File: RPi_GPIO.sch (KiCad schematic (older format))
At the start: 39 parts, among them J2 RPi_GPIO, J3 Conn_02x03_Counter_Clockwise, J4 Conn_01x02_Male, J5 Conn_01x03_Male, J6 Conn_01x03_Male, J7 Conn_01x03_Male, J8 Conn_01x03_Male, SW1 SW_Push, U2 STM32F030CCTx, U3 MAX485E, U4 MAX485E, U5 MAX485E, U6 MAX485E

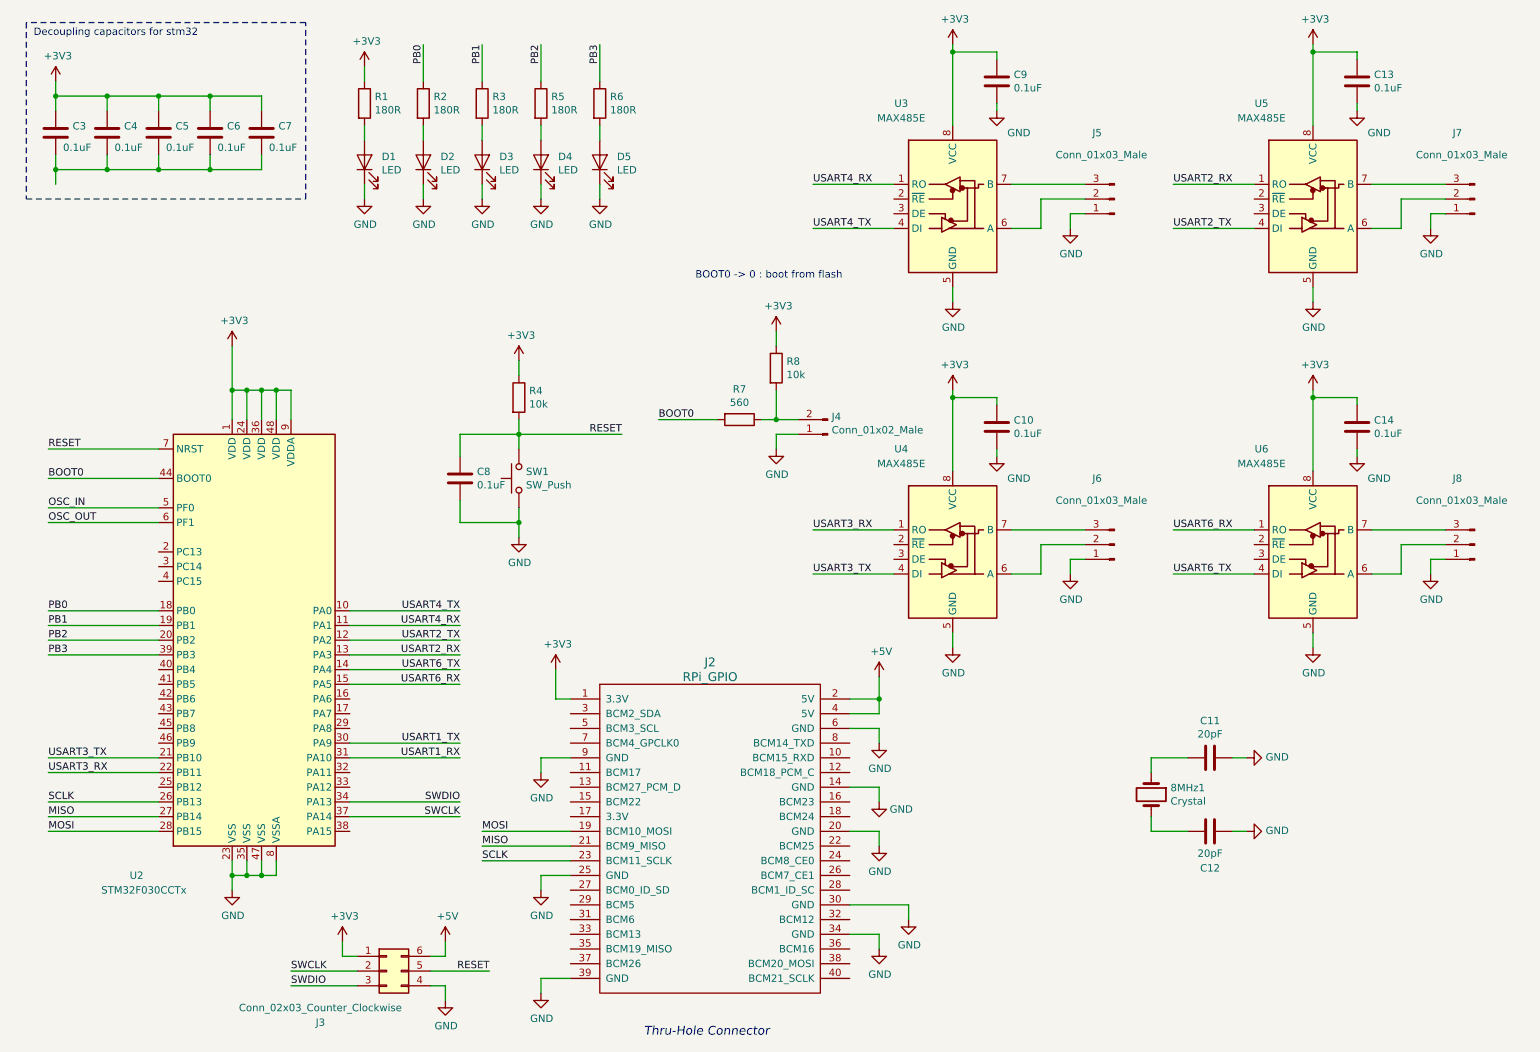
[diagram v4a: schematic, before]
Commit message: Correct DRC and add nmea interface
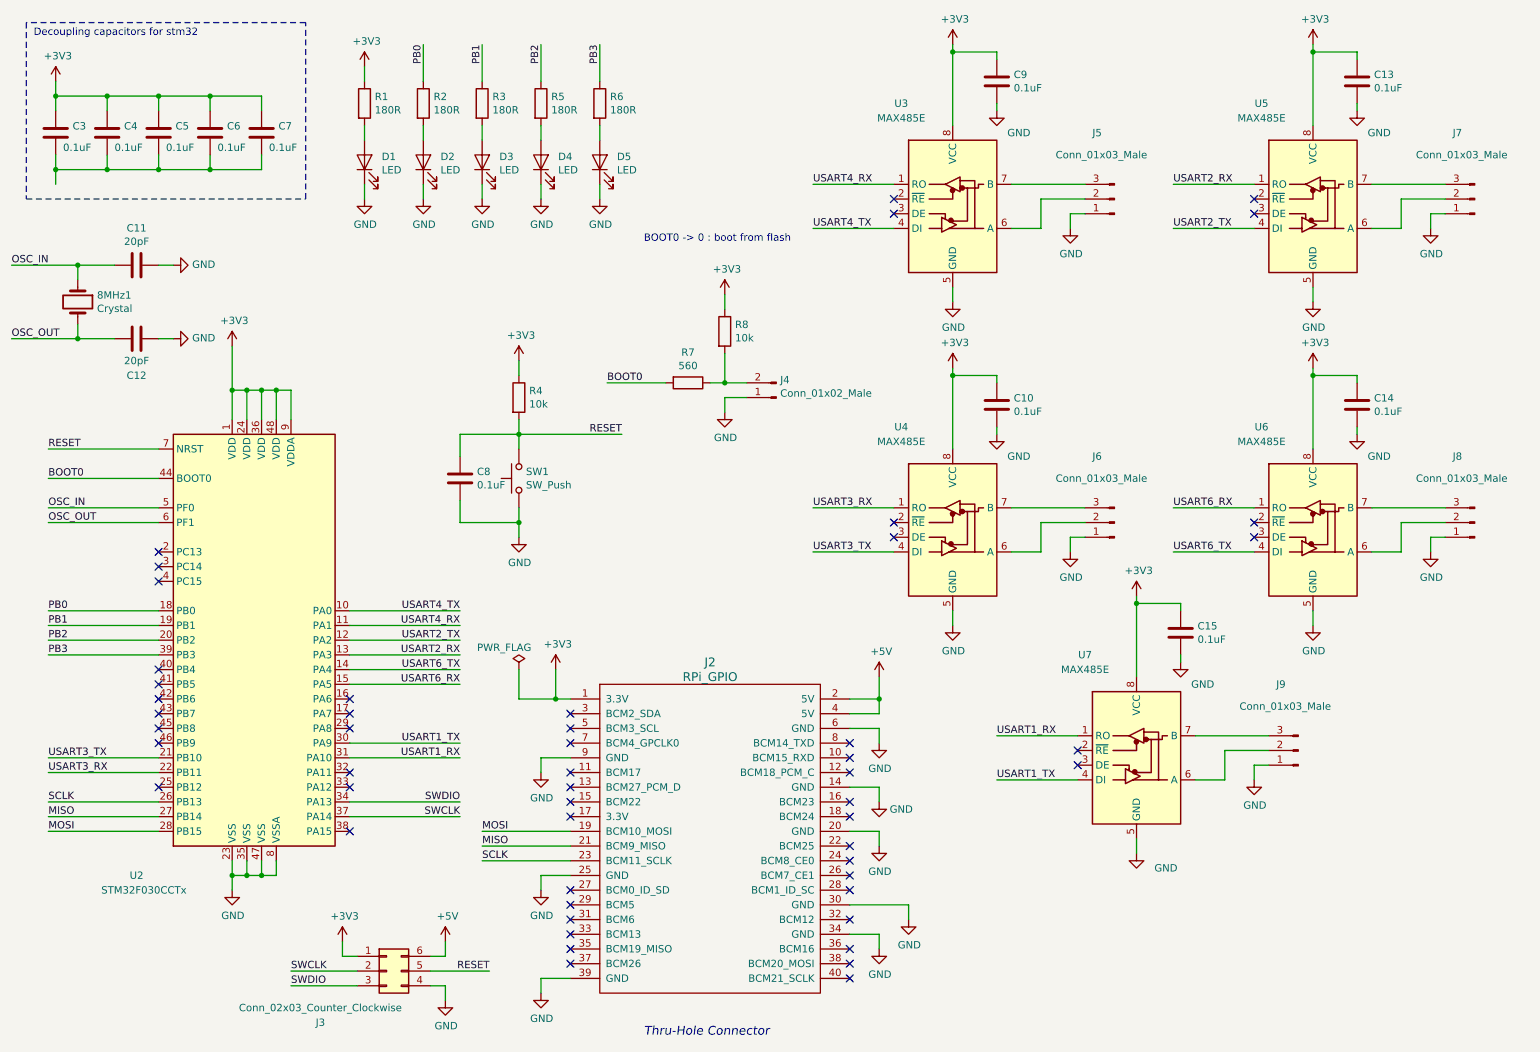
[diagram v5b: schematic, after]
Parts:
- added C15: 0.1uF, Capacitors_SMD:C_0603_HandSoldering, symbol Device:C
- added J9: Conn_01x03_Male, Connectors_JST:JST_ACH_BM03B-ACHSS_03x1.20mm_Angled, symbol Connector:Conn_01x03_Male
- added U7: MAX485E, digikey-footprints:SOIC-8_W3.9mm, symbol Interface_UART:MAX485E
- J5, J6, J7, J8: footprint (none) -> Connectors_JST:JST_ACH_BM03B-ACHSS_03x1.20mm_Angled; dkReference ED2819-ND -> 455-1579-1-ND
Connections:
- net +3V3: now also C15.1, U7.8 (VCC)
- net GND: now also C15.2, J9.1 (Pin_1), U7.5 (GND)
- net OSC_IN: now also 8MHz1.1, C11.2
- net OSC_OUT: now also 8MHz1.2, C12.2
- net USART1_RX: now also U7.1 (RO)
- net USART1_TX: now also U7.4 (DI)
- new net: J9.2 (Pin_2), U7.6 (A)
- new net: J9.3 (Pin_3), U7.7 (B)
- no-connect marks 0 -> 52
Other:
- moved on the sheet: 8MHz1, C10, C11, C12, C14, J4, J6, J8, R7, R8, U4, U6

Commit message: Finish schem and start routing
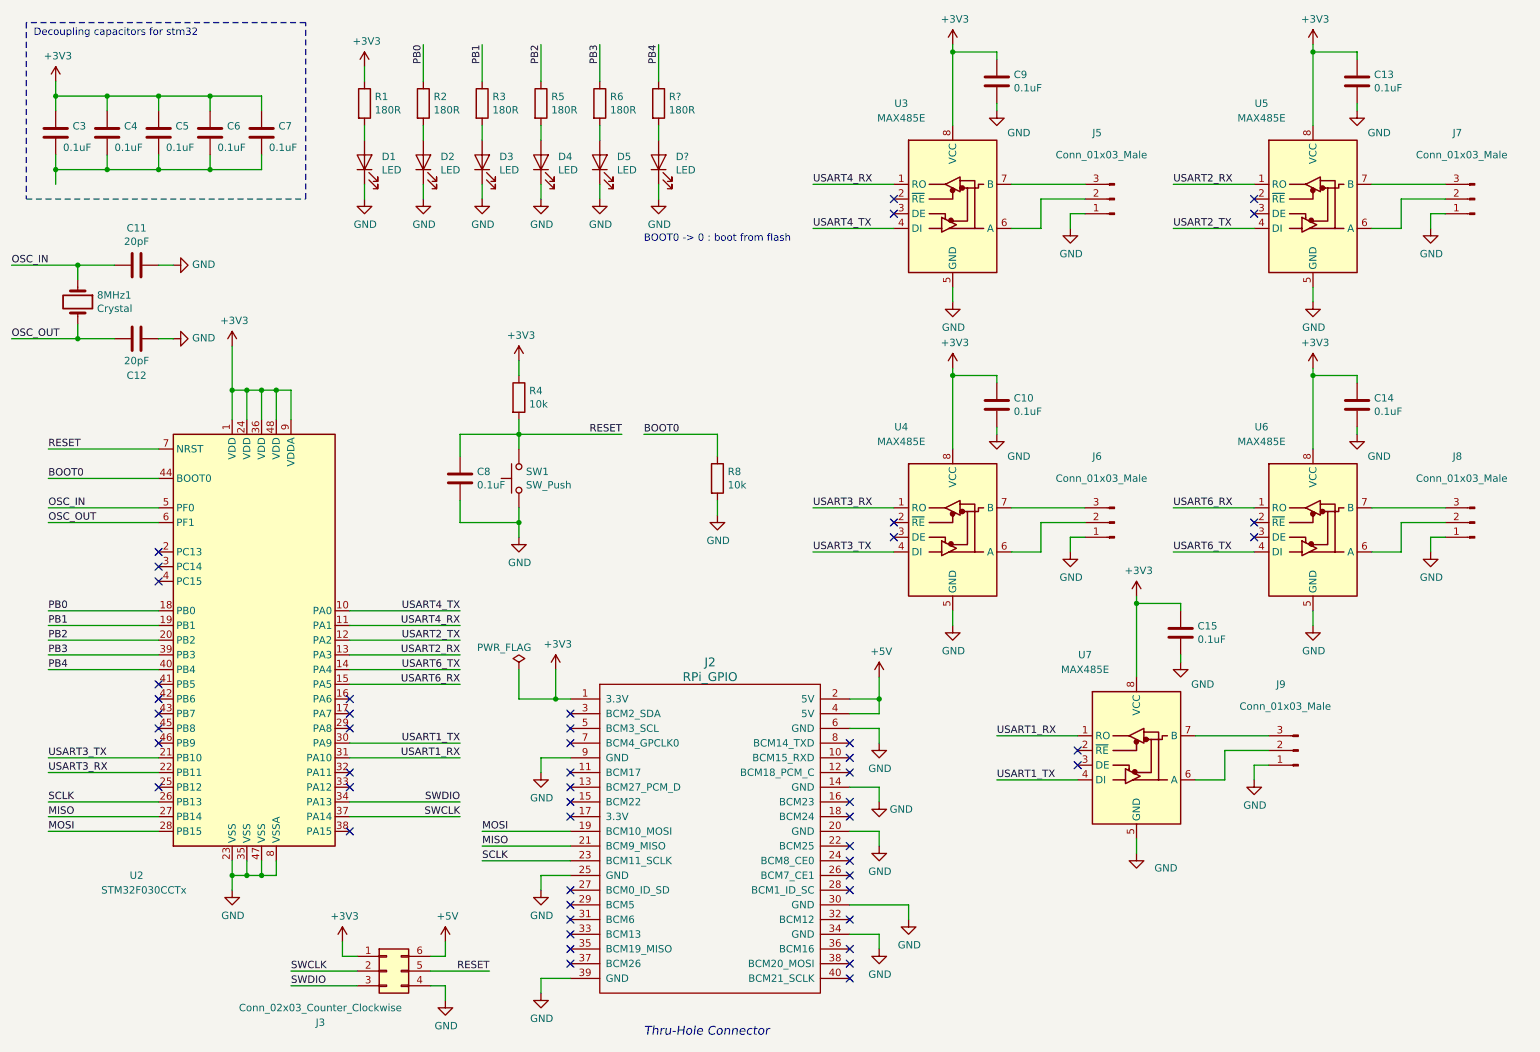
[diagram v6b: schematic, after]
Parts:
- removed J4: Conn_01x02_Male, symbol Connector:Conn_01x02_Male
- removed R7: 560, LEDs:LED_0603_HandSoldering, symbol Device:R
- added D?: LED, LEDs:LED_0603_HandSoldering, symbol Device:LED
- added R?: 180R, Resistors_SMD:R_0603_HandSoldering, symbol Device:R
- J3: footprint (none) -> Connectors_Samtec:SDL-106-X-XX_2x03
- J5, J6, J7, J8, J9: footprint Connectors_JST:JST_ACH_BM03B-ACHSS_03x1.20mm_Angled -> Connectors_JST:JST_SH_SM03B-SRSS-TB_03x1.00mm_Angled; dkReference 455-1579-1-ND -> 455-1803-1-ND
- U2: footprint Package_QFP:LQFP-48_7x7mm_P0.5mm -> digikey-footprints:LQFP-48_7x7mm
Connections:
- net +3V3: no longer R8.1
- net BOOT0: now also R8.1
- net GND: now also R8.2, D?.1 (K)
- net PB4: now reaches U2.40 (PB4)
- net PB4: now also R?.1
- new net: D?.2 (A), R?.2
- no-connect marks 52 -> 51
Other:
- moved on the sheet: R8
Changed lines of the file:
@@
 F 0 "U2" H 1550 3300 50  0000 C CNN
 F 1 "STM32F030CCTx" H 1600 3200 50  0000 C CNN
-F 2 "Package_QFP:LQFP-48_7x7mm_P0.5mm" H 1800 3500 50  0001 R CNN
+F 2 "digikey-footprints:LQFP-48_7x7mm" H 1800 3500 50  0001 R CNN
 F 3 "http://www.st.com/st-web-ui/static/active/en/resource/technical/document/datasheet/DM00088500.pdf" H 2400 4900 50  0001 C CNN
 F 4 "497-17296-ND" H 2400 4900 50  0001 C CNN "dkReference"
@@
 Text Label 950  3800 0    50   ~ 0
 BOOT0
-$Comp
-L power:GND #PWR?
-U 1 1 5C4AB0B1
-P 5550 3350
-F 0 "#PWR?" H 5550 3100 50  0001 C CNN
-F 1 "GND" H 5555 3177 50  0000 C CNN
-F 2 "" H 5550 3350 50  0001 C CNN
-F 3 "" H 5550 3350 50  0001 C CNN
-	1    5550 3350
-	1    0    0    -1
-$EndComp
 Text Notes 6000 2200 2    50   ~ 0
 BOOT0 -> 0 : boot from flash
@@
 F 0 "J5" H 8350 1450 50  0000 R CNN
 F 1 "Conn_01x03_Male" H 8600 1600 50  0000 R CNN
-F 2 "Connectors_JST:JST_ACH_BM03B-ACHSS_03x1.20mm_Angled" H 8200 1900 50  0001 C CNN
+F 2 "Connectors_JST:JST_SH_SM03B-SRSS-TB_03x1.00mm_Angled" H 8200 1900 50  0001 C CNN
 F 3 "~" H 8200 1900 50  0001 C CNN
-F 4 "455-1579-1-ND" H 0   0   50  0001 C CNN "dkReference"
+F 4 "455-1803-1-ND" H 0   0   50  0001 C CNN "dkReference"
 	1    8200 1900
 	-1   0    0    1
@@
 F 0 "J7" H 10800 1450 50  0000 R CNN
 F 1 "Conn_01x03_Male" H 11050 1600 50  0000 R CNN
-F 2 "Connectors_JST:JST_ACH_BM03B-ACHSS_03x1.20mm_Angled" H 10650 1900 50  0001 C CNN
+F 2 "Connectors_JST:JST_SH_SM03B-SRSS-TB_03x1.00mm_Angled" H 10650 1900 50  0001 C CNN
 F 3 "~" H 10650 1900 50  0001 C CNN
-F 4 "455-1579-1-ND" H 0   0   50  0001 C CNN "dkReference"
+F 4 "455-1803-1-ND" H 0   0   50  0001 C CNN "dkReference"
 	1    10650 1900
 	-1   0    0    1
@@
 F 0 "J6" H 8350 3650 50  0000 R CNN
 F 1 "Conn_01x03_Male" H 8600 3800 50  0000 R CNN
-F 2 "Connectors_JST:JST_ACH_BM03B-ACHSS_03x1.20mm_Angled" H 8200 4100 50  0001 C CNN
+F 2 "Connectors_JST:JST_SH_SM03B-SRSS-TB_03x1.00mm_Angled" H 8200 4100 50  0001 C CNN
 F 3 "~" H 8200 4100 50  0001 C CNN
-F 4 "455-1579-1-ND" H 0   -150 50  0001 C CNN "dkReference"
+F 4 "455-1803-1-ND" H 0   -150 50  0001 C CNN "dkReference"
 	1    8200 4100
 	-1   0    0    1
@@
 F 0 "J8" H 10800 3650 50  0000 R CNN
 F 1 "Conn_01x03_Male" H 11050 3800 50  0000 R CNN
-F 2 "Connectors_JST:JST_ACH_BM03B-ACHSS_03x1.20mm_Angled" H 10650 4100 50  0001 C CNN
+F 2 "Connectors_JST:JST_SH_SM03B-SRSS-TB_03x1.00mm_Angled" H 10650 4100 50  0001 C CNN
 F 3 "~" H 10650 4100 50  0001 C CNN
-F 4 "455-1579-1-ND" H 0   -150 50  0001 C CNN "dkReference"
+F 4 "455-1803-1-ND" H 0   -150 50  0001 C CNN "dkReference"
 	1    10650 4100
 	-1   0    0    1
@@
 F 0 "J3" H 2800 6800 50  0000 C CNN
 F 1 "Conn_02x03_Counter_Clockwise" H 2800 6900 50  0000 C CNN
-F 2 "" H 3250 7150 50  0001 C CNN
+F 2 "Connectors_Samtec:SDL-106-X-XX_2x03" H 3250 7150 50  0001 C CNN
 F 3 "~" H 3250 7150 50  0001 C CNN
 	1    3250 7150
@@
 	1    0    0    -1
 $EndComp
-Text Label 4750 3150 0    50   ~ 0
+Text Label 5000 3500 0    50   ~ 0
 BOOT0
-Wire Wire Line
-	5550 3250 5550 3350
 $Comp
 L Device:R R8
 U 1 1 5C658078
-P 5550 2800
-F 0 "R8" H 5620 2846 50  0000 L CNN
-F 1 "10k" H 5620 2755 50  0000 L CNN
-F 2 "Resistors_SMD:R_0603_HandSoldering" V 5480 2800 50  0001 C CNN
-F 3 "~" H 5550 2800 50  0001 C CNN
-F 4 "RMCF0201FT10K0CT-ND" H 5550 2800 50  0001 C CNN "dkReference"
-	1    5550 2800
-	1    0    0    -1
-$EndComp
-Wire Wire Line
-	5550 2650 5550 2550
-$Comp
-L power:+3V3 #PWR?
-U 1 1 5C66017C
-P 5550 2550
-F 0 "#PWR?" H 5550 2400 50  0001 C CNN
-F 1 "+3V3" H 5565 2723 50  0000 C CNN
-F 2 "" H 5550 2550 50  0001 C CNN
-F 3 "" H 5550 2550 50  0001 C CNN
-	1    5550 2550
+P 5500 3800
+F 0 "R8" H 5570 3846 50  0000 L CNN
+F 1 "10k" H 5570 3755 50  0000 L CNN
+F 2 "Resistors_SMD:R_0603_HandSoldering" V 5430 3800 50  0001 C CNN
+F 3 "~" H 5500 3800 50  0001 C CNN
+F 4 "RMCF0201FT10K0CT-ND" H 5500 3800 50  0001 C CNN "dkReference"
+	1    5500 3800
 	1    0    0    -1
 $EndComp
@@
 	0    -1   -1   0
 $EndComp
-Wire Wire Line
-	5550 2950 5550 3150
-$Comp
-L Connector:Conn_01x02_Male J4
-U 1 1 5C6B4A6B
-P 5900 3250
-F 0 "J4" H 5873 3130 50  0000 R CNN
-F 1 "Conn_01x02_Male" H 5873 3221 50  0000 R CNN
-F 2 "" H 5900 3250 50  0001 C CNN
-F 3 "~" H 5900 3250 50  0001 C CNN
-F 4 "ED2819-ND" H -350 -250 50  0001 C CNN "dkReference"
-	1    5900 3250
-	-1   0    0    1
-$EndComp
-Wire Wire Line
-	5700 3150 5550 3150
-Wire Wire Line
-	5550 3250 5700 3250
-Wire Wire Line
-	5550 3150 5450 3150
-Connection ~ 5550 3150
-$Comp
-L Device:R R7
-U 1 1 5C6D6442
-P 5300 3150
-F 0 "R7" V 5093 3150 50  0000 C CNN
-F 1 "560" V 5184 3150 50  0000 C CNN
-F 2 "LEDs:LED_0603_HandSoldering" V 5230 3150 50  0001 C CNN
-F 3 "~" H 5300 3150 50  0001 C CNN
-F 4 "RC0201JR-07560RL" V 5300 3150 50  0001 C CNN "dkReference"
-	1    5300 3150
-	0    1    1    0
-$EndComp
-Wire Wire Line
-	5150 3150 4750 3150
 NoConn ~ 6400 5600
 NoConn ~ 6400 5700
@@
 NoConn ~ 1700 5300
 NoConn ~ 1700 5200
-NoConn ~ 1700 5100
 NoConn ~ 1700 4500
 NoConn ~ 1700 4400
@@
 F 0 "J9" H 9600 5200 50  0000 R CNN
 F 1 "Conn_01x03_Male" H 9850 5350 50  0000 R CNN
-F 2 "Connectors_JST:JST_ACH_BM03B-ACHSS_03x1.20mm_Angled" H 9450 5650 50  0001 C CNN
+F 2 "Connectors_JST:JST_SH_SM03B-SRSS-TB_03x1.00mm_Angled" H 9450 5650 50  0001 C CNN
 F 3 "~" H 9450 5650 50  0001 C CNN
-F 4 "455-1579-1-ND" H -1200 1400 50  0001 C CNN "dkReference"
+F 4 "455-1803-1-ND" H -1200 1400 50  0001 C CNN "dkReference"
 	1    9450 5650
 	-1   0    0    1
@@
 	1    0    0    -1
 $EndComp
+Wire Wire Line
+	5500 3500 5500 3650
+Wire Wire Line
+	5000 3500 5500 3500
+Wire Wire Line
+	5500 3950 5500 4050
+$Comp
+L power:GND #PWR?
+U 1 1 5C736817
+P 5500 4050
+F 0 "#PWR?" H 5500 3800 50  0001 C CNN
+F 1 "GND" H 5505 3877 50  0000 C CNN
+F 2 "" H 5500 4050 50  0001 C CNN
+F 3 "" H 5500 4050 50  0001 C CNN
+	1    5500 4050
+	1    0    0    -1
+$EndComp
+$Comp
+L Device:R R?
+U 1 1 5C528FF5
+P 5100 1250
+F 0 "R?" H 5170 1296 50  0000 L CNN
+F 1 "180R" H 5170 1205 50  0000 L CNN
+F 2 "Resistors_SMD:R_0603_HandSoldering" V 5030 1250 50  0001 C CNN
+F 3 "~" H 5100 1250 50  0001 C CNN
+F 4 "YAG2450CT-ND" H 5100 1250 50  0001 C CNN "dkReference"
+	1    5100 1250
+	1    0    0    -1
+$EndComp
+Wire Wire Line
+	5100 1100 5100 850
+Wire Wire Line
+	5100 1400 5100 1500
+$Comp
+L Device:LED D?
+U 1 1 5C528FFF
+P 5100 1650
+F 0 "D?" V 5138 1533 50  0000 R CNN
+F 1 "LED" V 5047 1533 50  0000 R CNN
+F 2 "LEDs:LED_0603_HandSoldering" H 5100 1650 50  0001 C CNN
+F 3 "~" H 5100 1650 50  0001 C CNN
+F 4 "SML-D12U1WT86CT-ND" V 5100 1650 50  0001 C CNN "dkReference"
+	1    5100 1650
+	0    -1   -1   0
+$EndComp
+Wire Wire Line
+	5100 1800 5100 1900
+$Comp
+L power:GND #PWR?
+U 1 1 5C529007
+P 5100 1900
+F 0 "#PWR?" H 5100 1650 50  0001 C CNN
+F 1 "GND" H 5105 1727 50  0000 C CNN
+F 2 "" H 5100 1900 50  0001 C CNN
+F 3 "" H 5100 1900 50  0001 C CNN
+	1    5100 1900
+	1    0    0    -1
+$EndComp
+Text Label 5100 850  3    50   ~ 0
+PB4
+Wire Wire Line
+	1700 5100 950  5100
+Text Label 950  5100 0    50   ~ 0
+PB4
 $EndSCHEMATC

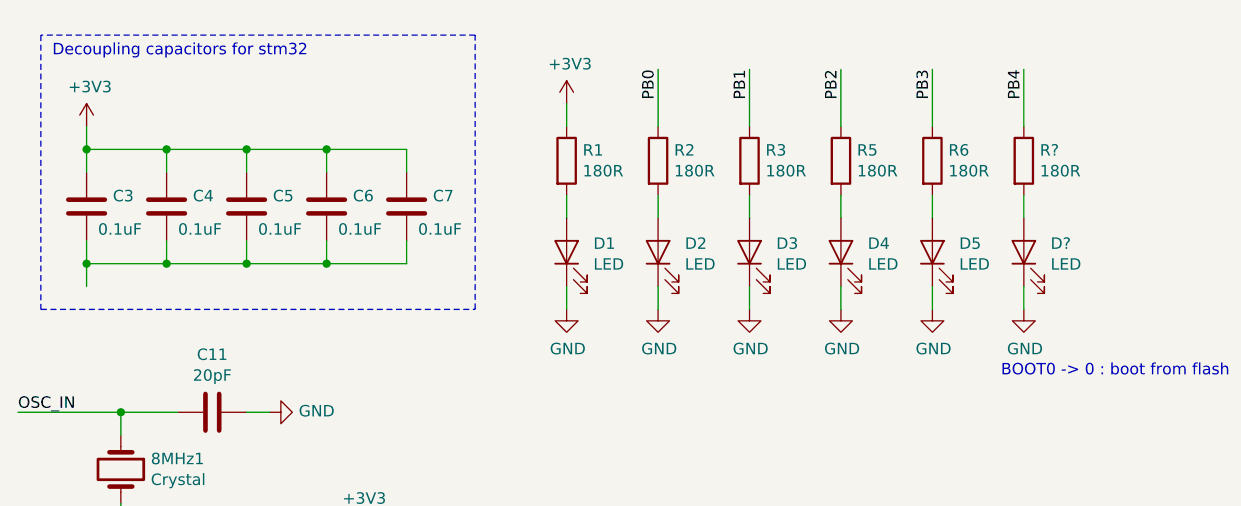
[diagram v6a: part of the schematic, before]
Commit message: Update footprints, fix gnd missing, start to align connectors
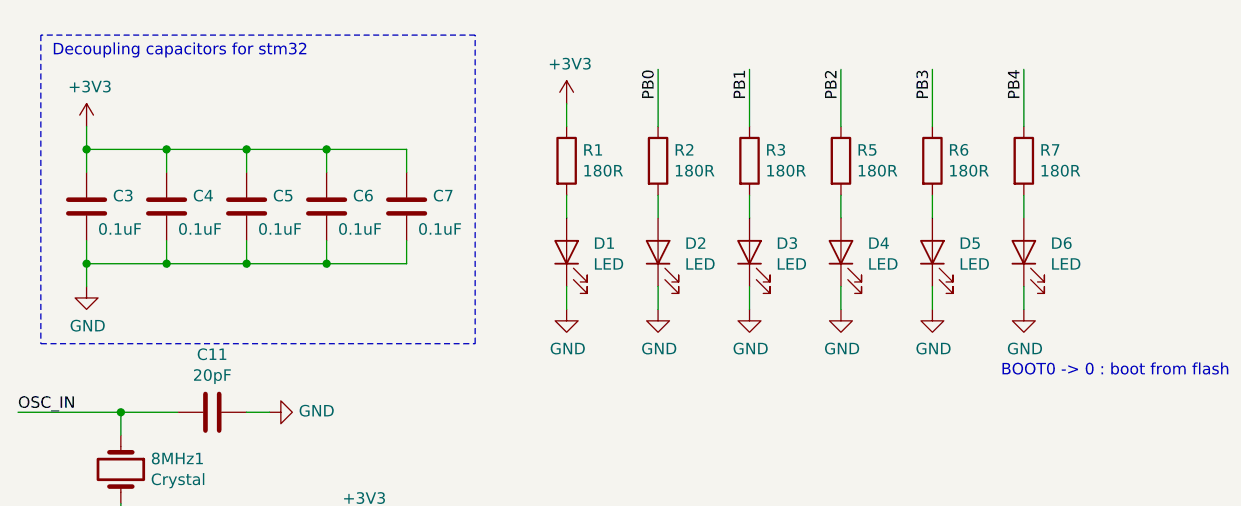
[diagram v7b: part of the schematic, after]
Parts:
- gave numbers to parts that had none: 2
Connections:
- net GND: now also C3.2, C4.2, C5.2, C6.2, C7.2
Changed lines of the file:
@@
 	1350 1700 1700 1700
 Wire Notes Line
-	800  1900 2700 1900
+	800  2050 2700 2050
 Wire Notes Line
-	2700 1900 2700 700
+	2700 2050 2700 700
 Wire Notes Line
 	2700 700  800  700
 Wire Notes Line
-	800  700  800  1900
+	800  700  800  2050
 Text Notes 850  800  0    50   ~ 0
 Decoupling capacitors for stm32\n
@@
 $EndComp
 $Comp
-L Device:R R?
+L Device:R R7
 U 1 1 5C528FF5
 P 5100 1250
-F 0 "R?" H 5170 1296 50  0000 L CNN
+F 0 "R7" H 5170 1296 50  0000 L CNN
 F 1 "180R" H 5170 1205 50  0000 L CNN
 F 2 "Resistors_SMD:R_0603_HandSoldering" V 5030 1250 50  0001 C CNN
@@
 	5100 1400 5100 1500
 $Comp
-L Device:LED D?
+L Device:LED D6
 U 1 1 5C528FFF
 P 5100 1650
-F 0 "D?" V 5138 1533 50  0000 R CNN
+F 0 "D6" V 5138 1533 50  0000 R CNN
 F 1 "LED" V 5047 1533 50  0000 R CNN
 F 2 "LEDs:LED_0603_HandSoldering" H 5100 1650 50  0001 C CNN
@@
 Text Label 950  5100 0    50   ~ 0
 PB4
+$Comp
+L power:GND #PWR?
+U 1 1 5C5EA05C
+P 1000 1800
+F 0 "#PWR?" H 1000 1550 50  0001 C CNN
+F 1 "GND" H 1005 1627 50  0000 C CNN
+F 2 "" H 1000 1800 50  0001 C CNN
+F 3 "" H 1000 1800 50  0001 C CNN
+	1    1000 1800
+	1    0    0    -1
+$EndComp
 $EndSCHEMATC
